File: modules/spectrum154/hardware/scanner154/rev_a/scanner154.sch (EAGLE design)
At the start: 8 parts, among them J1 TC2030-CC2538-BL, J2 MODULE_HEADER, U1 ATUM, U2 MAX8887EZK33+T

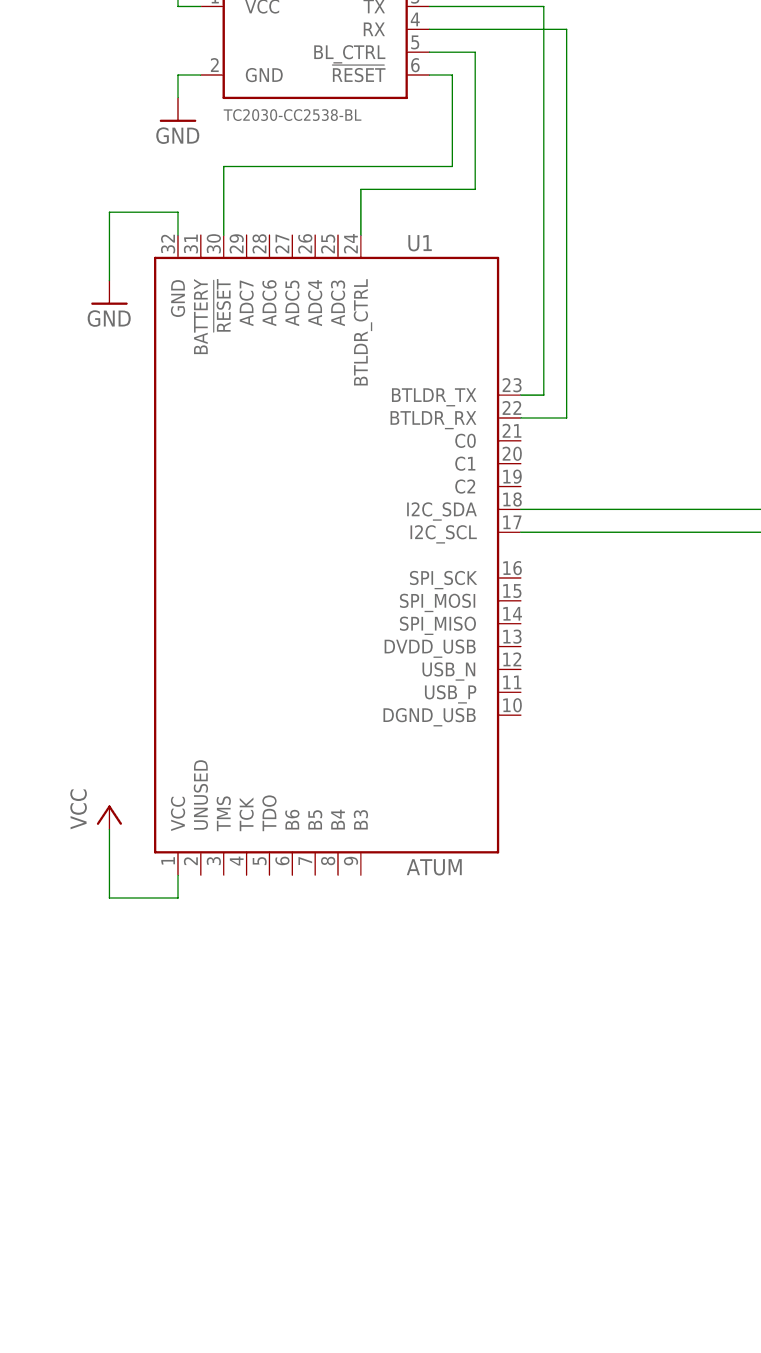
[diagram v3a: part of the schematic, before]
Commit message: add debugging header to 154 scanner
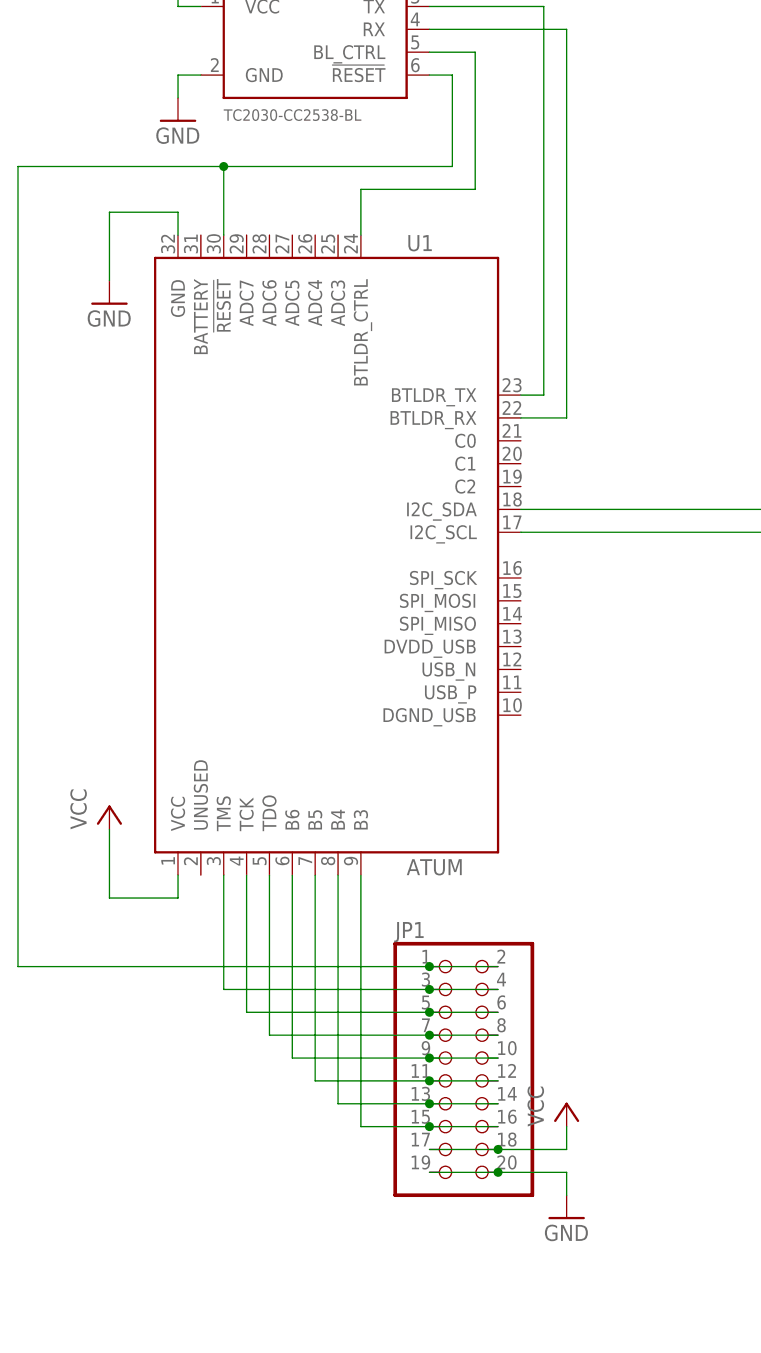
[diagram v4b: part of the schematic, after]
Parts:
- added JP1: (no value), pinhead:PINHD-2X10
- C1: DIGIKEY (none) -> 490-1512-1-ND
- C2, C3: DIGIKEY (none) -> 490-3297-1-ND
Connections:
- net N$2 renamed SDA
- net N$3 renamed SCL
- net VBAT renamed 5V
- removed net N$8: J1.!RESET, U1.!RESET
- new net !RESET: J1.!RESET, JP1.1, JP1.2, U1.!RESET
- new net B3: JP1.15, JP1.16, U1.B3
- new net B4: JP1.13, JP1.14, U1.B4
- new net B5: JP1.11, JP1.12, U1.B5
- new net B6: JP1.10, JP1.9, U1.B6
- new net TCK: JP1.5, JP1.6, U1.TCK
- new net TDO: JP1.7, JP1.8, U1.TDO
- new net TMS: JP1.3, JP1.4, U1.TMS
- net GND: now also JP1.19, JP1.20
- net VCC: now also JP1.17, JP1.18
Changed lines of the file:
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@@
 <part name="J2" library="signpost" deviceset="MODULE_HEADER" device=""/>
 <part name="SUPPLY3" library="supply1" deviceset="GND" device=""/>
-<part name="C1" library="passives" deviceset="CAPACITOR" device="0603_CAP" value="10nF"/>
-<part name="C2" library="passives" deviceset="CAPACITOR" device="0603_CAP" value="4.7uF"/>
-<part name="C3" library="passives" deviceset="CAPACITOR" device="0603_CAP" value="4.7uF"/>
+<part name="C1" library="passives" deviceset="CAPACITOR" device="0603_CAP" value="10nF">
+<attribute name="DIGIKEY" value="490-1512-1-ND"/>
+</part>
+<part name="C2" library="passives" deviceset="CAPACITOR" device="0603_CAP" value="4.7uF">
+<attribute name="DIGIKEY" value="490-3297-1-ND"/>
+</part>
+<part name="C3" library="passives" deviceset="CAPACITOR" device="0603_CAP" value="4.7uF">
+<attribute name="DIGIKEY" value="490-3297-1-ND"/>
+</part>
 <part name="LOGO2" library="logos" deviceset="UMICH_SOLID" device="_HUGE"/>
 <part name="P+4" library="supply1" deviceset="VCC" device=""/>
+<part name="JP1" library="pinhead" deviceset="PINHD-2X10" device=""/>
+<part name="P+5" library="supply1" deviceset="VCC" device=""/>
+<part name="SUPPLY4" library="supply1" deviceset="GND" device=""/>
 </parts>
 <sheets>
@@
 <instance part="J2" gate="G$1" x="134.62" y="137.16"/>
 <instance part="SUPPLY3" gate="1" x="142.24" y="119.38"/>
-<instance part="C1" gate="G$1" x="205.74" y="137.16"/>
-<instance part="C2" gate="G$1" x="172.72" y="137.16"/>
-<instance part="C3" gate="G$1" x="215.9" y="137.16"/>
+<instance part="C1" gate="G$1" x="205.74" y="137.16">
+<attribute name="DIGIKEY" x="205.74" y="137.16" size="1.778" layer="96" display="off"/>
+</instance>
+<instance part="C2" gate="G$1" x="172.72" y="137.16">
+<attribute name="DIGIKEY" x="172.72" y="137.16" size="1.778" layer="96" display="off"/>
+</instance>
+<instance part="C3" gate="G$1" x="215.9" y="137.16">
+<attribute name="DIGIKEY" x="215.9" y="137.16" size="1.778" layer="96" display="off"/>
+</instance>
 <instance part="LOGO2" gate="G$1" x="231.14" y="25.4"/>
 <instance part="P+4" gate="VCC" x="142.24" y="165.1"/>
+<instance part="JP1" gate="A" x="73.66" y="30.48"/>
+<instance part="P+5" gate="VCC" x="86.36" y="25.4"/>
+<instance part="SUPPLY4" gate="1" x="86.36" y="12.7"/>
 </instances>
 <busses>
@@
 <wire x1="142.24" y1="124.46" x2="142.24" y2="121.92" width="0.1524" layer="91"/>
 <pinref part="SUPPLY3" gate="1" pin="GND"/>
+</segment>
+<segment>
+<pinref part="JP1" gate="A" pin="19"/>
+<pinref part="JP1" gate="A" pin="20"/>
+<wire x1="71.12" y1="17.78" x2="78.74" y2="17.78" width="0.1524" layer="91"/>
+<wire x1="78.74" y1="17.78" x2="86.36" y2="17.78" width="0.1524" layer="91"/>
+<junction x="78.74" y="17.78"/>
+<wire x1="86.36" y1="17.78" x2="86.36" y2="15.24" width="0.1524" layer="91"/>
+<pinref part="SUPPLY4" gate="1" pin="GND"/>
 </segment>
 </net>
@@
 <wire x1="142.24" y1="154.94" x2="142.24" y2="162.56" width="0.1524" layer="91"/>
 </segment>
-</net>
-<net name="VBAT" class="0">
+<segment>
+<pinref part="JP1" gate="A" pin="18"/>
+<pinref part="JP1" gate="A" pin="17"/>
+<wire x1="78.74" y1="20.32" x2="71.12" y2="20.32" width="0.1524" layer="91"/>
+<wire x1="78.74" y1="20.32" x2="86.36" y2="20.32" width="0.1524" layer="91"/>
+<junction x="78.74" y="20.32"/>
+<wire x1="86.36" y1="20.32" x2="86.36" y2="22.86" width="0.1524" layer="91"/>
+<pinref part="P+5" gate="VCC" pin="VCC"/>
+</segment>
+</net>
+<net name="5V" class="0">
 <segment>
 <wire x1="172.72" y1="139.7" x2="172.72" y2="142.24" width="0.1524" layer="91"/>
@@
 </segment>
 </net>
-<net name="N$8" class="0">
+<net name="!RESET" class="0">
 <segment>
 <pinref part="U1" gate="G$1" pin="!RESET"/>
@@
 <pinref part="J1" gate="G$1" pin="!RESET"/>
 <wire x1="73.66" y1="139.7" x2="71.12" y2="139.7" width="0.1524" layer="91"/>
-</segment>
-</net>
-<net name="N$2" class="0">
+<pinref part="JP1" gate="A" pin="1"/>
+<wire x1="71.12" y1="40.64" x2="25.4" y2="40.64" width="0.1524" layer="91"/>
+<wire x1="25.4" y1="40.64" x2="25.4" y2="129.54" width="0.1524" layer="91"/>
+<wire x1="25.4" y1="129.54" x2="48.26" y2="129.54" width="0.1524" layer="91"/>
+<junction x="48.26" y="129.54"/>
+<pinref part="JP1" gate="A" pin="2"/>
+<wire x1="71.12" y1="40.64" x2="78.74" y2="40.64" width="0.1524" layer="91"/>
+<junction x="71.12" y="40.64"/>
+</segment>
+</net>
+<net name="SDA" class="0">
 <segment>
 <pinref part="J2" gate="G$1" pin="SDA"/>
@@
 </segment>
 </net>
-<net name="N$3" class="0">
+<net name="SCL" class="0">
 <segment>
 <pinref part="J2" gate="G$1" pin="SCL"/>
@@
 </segment>
 </net>
+<net name="TMS" class="0">
+<segment>
+<pinref part="JP1" gate="A" pin="3"/>
+<pinref part="JP1" gate="A" pin="4"/>
+<wire x1="71.12" y1="38.1" x2="78.74" y2="38.1" width="0.1524" layer="91"/>
+<pinref part="U1" gate="G$1" pin="TMS"/>
+<wire x1="71.12" y1="38.1" x2="48.26" y2="38.1" width="0.1524" layer="91"/>
+<wire x1="48.26" y1="38.1" x2="48.26" y2="50.8" width="0.1524" layer="91"/>
+<junction x="71.12" y="38.1"/>
+</segment>
+</net>
+<net name="TCK" class="0">
+<segment>
+<pinref part="JP1" gate="A" pin="5"/>
+<pinref part="JP1" gate="A" pin="6"/>
+<wire x1="71.12" y1="35.56" x2="78.74" y2="35.56" width="0.1524" layer="91"/>
+<pinref part="U1" gate="G$1" pin="TCK"/>
+<wire x1="50.8" y1="50.8" x2="50.8" y2="35.56" width="0.1524" layer="91"/>
+<wire x1="50.8" y1="35.56" x2="71.12" y2="35.56" width="0.1524" layer="91"/>
+<junction x="71.12" y="35.56"/>
+</segment>
+</net>
+<net name="TDO" class="0">
+<segment>
+<pinref part="JP1" gate="A" pin="8"/>
+<pinref part="JP1" gate="A" pin="7"/>
+<wire x1="78.74" y1="33.02" x2="71.12" y2="33.02" width="0.1524" layer="91"/>
+<pinref part="U1" gate="G$1" pin="TDO"/>
+<wire x1="53.34" y1="50.8" x2="53.34" y2="33.02" width="0.1524" layer="91"/>
+<wire x1="53.34" y1="33.02" x2="71.12" y2="33.02" width="0.1524" layer="91"/>
+<junction x="71.12" y="33.02"/>
+</segment>
+</net>
+<net name="B6" class="0">
+<segment>
+<pinref part="JP1" gate="A" pin="9"/>
+<pinref part="JP1" gate="A" pin="10"/>
+<wire x1="71.12" y1="30.48" x2="78.74" y2="30.48" width="0.1524" layer="91"/>
+<pinref part="U1" gate="G$1" pin="B6"/>
+<wire x1="55.88" y1="50.8" x2="55.88" y2="30.48" width="0.1524" layer="91"/>
+<wire x1="55.88" y1="30.48" x2="71.12" y2="30.48" width="0.1524" layer="91"/>
+<junction x="71.12" y="30.48"/>
+</segment>
+</net>
+<net name="B5" class="0">
+<segment>
+<pinref part="JP1" gate="A" pin="12"/>
+<pinref part="JP1" gate="A" pin="11"/>
+<wire x1="78.74" y1="27.94" x2="71.12" y2="27.94" width="0.1524" layer="91"/>
+<pinref part="U1" gate="G$1" pin="B5"/>
+<wire x1="58.42" y1="50.8" x2="58.42" y2="27.94" width="0.1524" layer="91"/>
+<wire x1="58.42" y1="27.94" x2="71.12" y2="27.94" width="0.1524" layer="91"/>
+<junction x="71.12" y="27.94"/>
+</segment>
+</net>
+<net name="B4" class="0">
+<segment>
+<pinref part="JP1" gate="A" pin="13"/>
+<pinref part="JP1" gate="A" pin="14"/>
+<wire x1="71.12" y1="25.4" x2="78.74" y2="25.4" width="0.1524" layer="91"/>
+<pinref part="U1" gate="G$1" pin="B4"/>
+<wire x1="60.96" y1="50.8" x2="60.96" y2="25.4" width="0.1524" layer="91"/>
+<wire x1="60.96" y1="25.4" x2="71.12" y2="25.4" width="0.1524" layer="91"/>
+<junction x="71.12" y="25.4"/>
+</segment>
+</net>
+<net name="B3" class="0">
+<segment>
+<pinref part="JP1" gate="A" pin="15"/>
+<pinref part="JP1" gate="A" pin="16"/>
+<wire x1="71.12" y1="22.86" x2="78.74" y2="22.86" width="0.1524" layer="91"/>
+<pinref part="U1" gate="G$1" pin="B3"/>
+<wire x1="63.5" y1="50.8" x2="63.5" y2="22.86" width="0.1524" layer="91"/>
+<wire x1="63.5" y1="22.86" x2="71.12" y2="22.86" width="0.1524" layer="91"/>
+<junction x="71.12" y="22.86"/>
+</segment>
+</net>
